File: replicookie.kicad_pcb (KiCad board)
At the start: 2 copper layers, 152.4 x 101.6 mm, 8 parts, among them P2 TFM-115-01-F-D-A, P3 TFM-120-01-F-D-A

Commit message: Annotate schematic
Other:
- net class Default removed

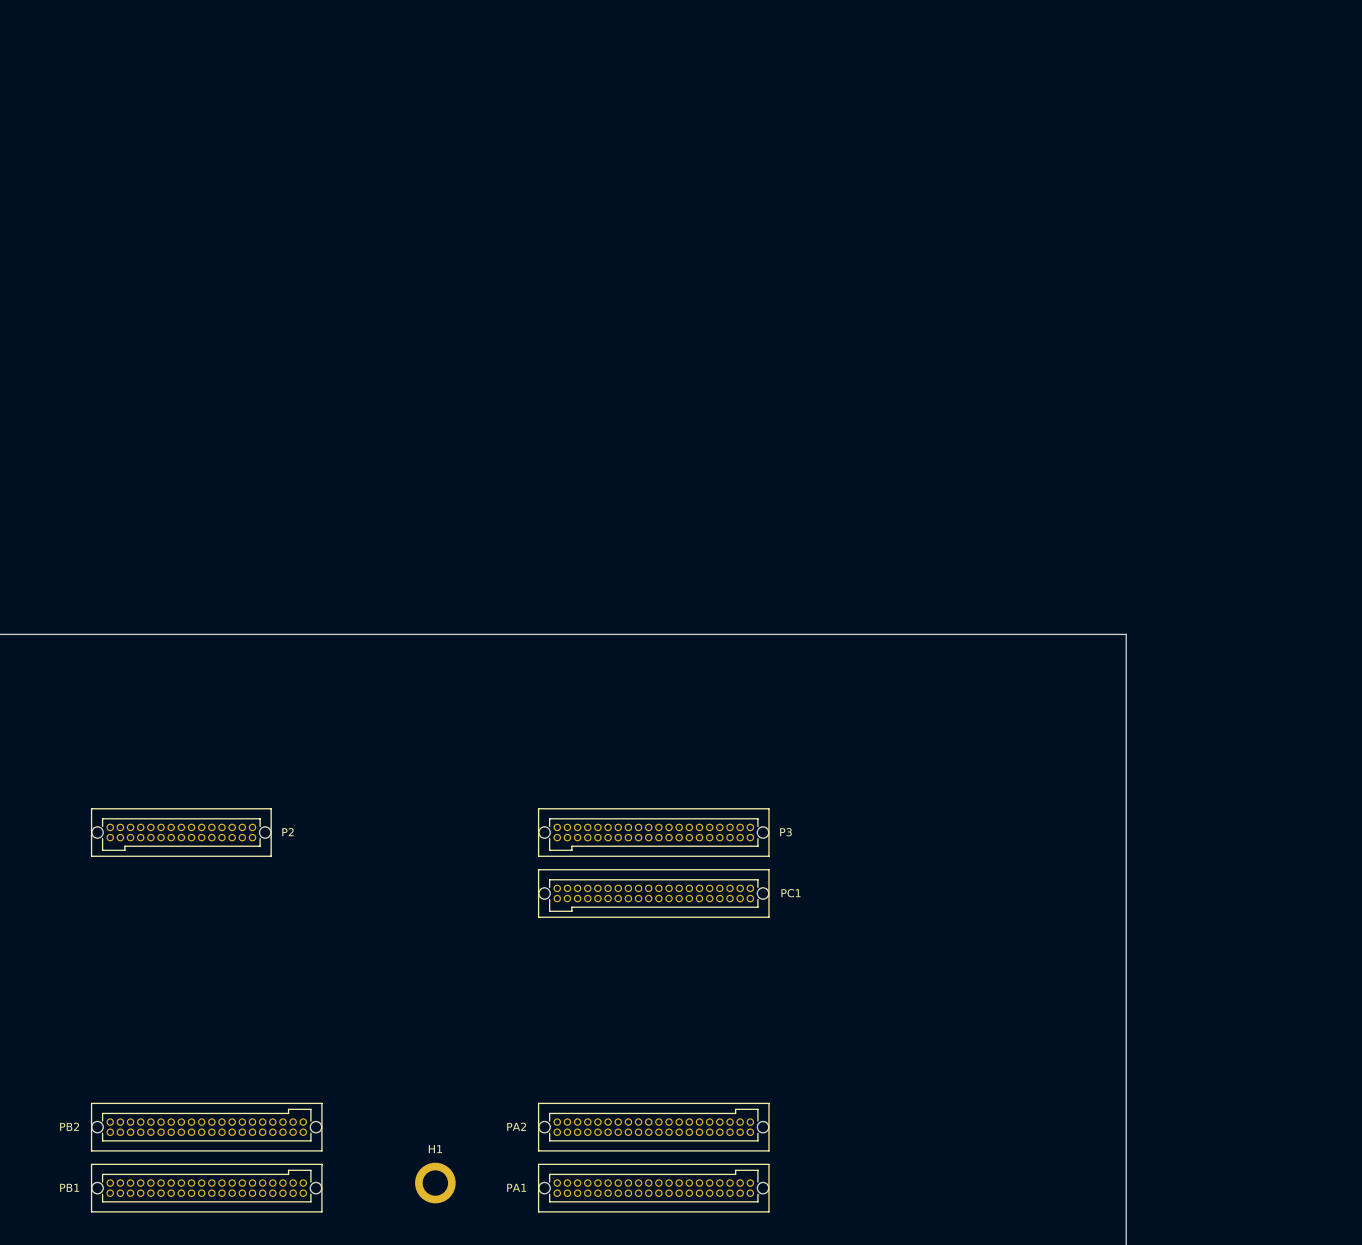
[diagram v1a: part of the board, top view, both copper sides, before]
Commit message: Fix footprint associations, use 74LVC2G07 instead of MOSFETs
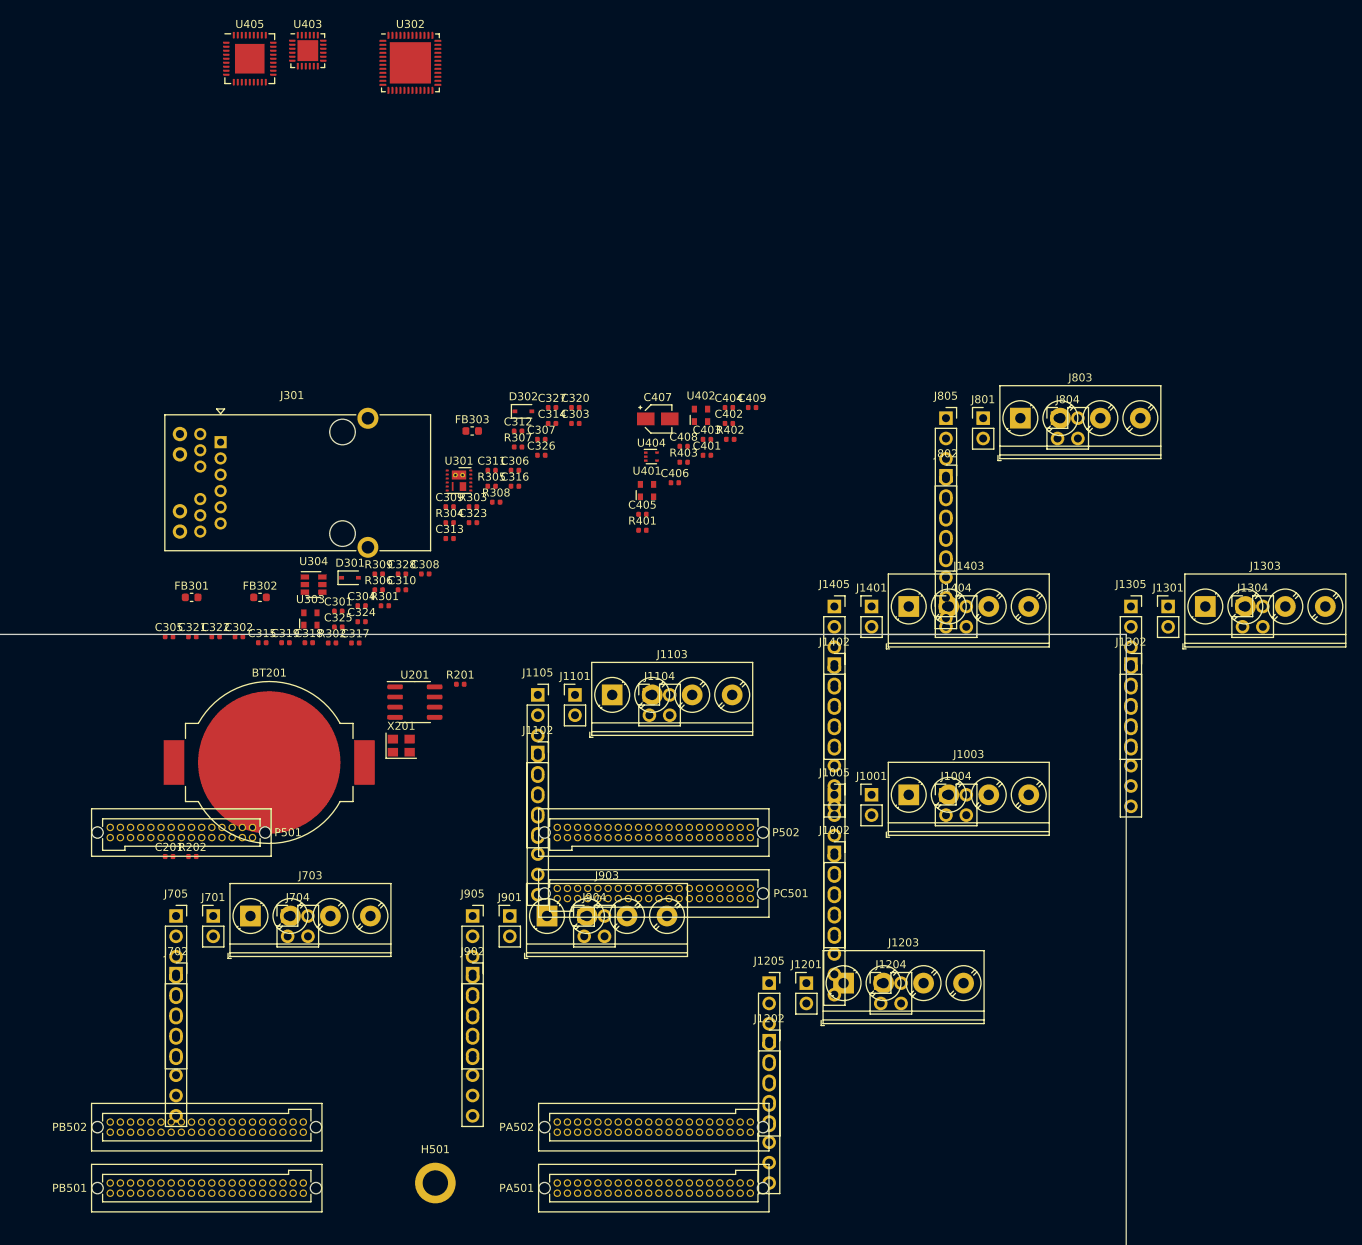
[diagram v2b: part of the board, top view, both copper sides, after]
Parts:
- added BT201: Battery_Cell, Battery:BatteryHolder_MPD_BC2003_1x2032, F.Cu at (83.4, 54.1)
- added C201: 0.01u, Capacitor_SMD:C_0402_1005Metric, F.Cu at (70.9, 65.9)
- added C301: 4.7u, Capacitor_SMD:C_0402_1005Metric, F.Cu at (92.0, 35.2)
- added C302: 560p, Capacitor_SMD:C_0402_1005Metric, F.Cu at (79.6, 38.4)
- added C303: 10u, Capacitor_SMD:C_0402_1005Metric, F.Cu at (121.6, 11.7)
- added C304: 10u, Capacitor_SMD:C_0402_1005Metric, F.Cu at (94.9, 34.5)
- added C305: 10u, Capacitor_SMD:C_0402_1005Metric, F.Cu at (70.9, 38.4)
- added C306: 0.1U, Capacitor_SMD:C_0402_1005Metric, F.Cu at (114.1, 17.6)
- added C307: 10u, Capacitor_SMD:C_0402_1005Metric, F.Cu at (117.4, 13.7)
- added C308: 10u, Capacitor_SMD:C_0402_1005Metric, F.Cu at (102.9, 30.5)
- added C309: 0.1U, Capacitor_SMD:C_0402_1005Metric, F.Cu at (105.9, 22.1)
- added C310: 0.1U, Capacitor_SMD:C_0402_1005Metric, F.Cu at (100.0, 32.5)
- added C311: 0.1U, Capacitor_SMD:C_0402_1005Metric, F.Cu at (111.2, 17.6)
- added C312: 0.1U, Capacitor_SMD:C_0402_1005Metric, F.Cu at (114.5, 12.7)
- added C313: 0.1U, Capacitor_SMD:C_0402_1005Metric, F.Cu at (105.9, 26.1)
- added C314: 0.1U, Capacitor_SMD:C_0402_1005Metric, F.Cu at (118.7, 11.7)
- added C315: 0.1U, Capacitor_SMD:C_0402_1005Metric, F.Cu at (82.5, 39.1)
- added C316: 0.1U, Capacitor_SMD:C_0402_1005Metric, F.Cu at (114.1, 19.6)
- added C317: 0.1U, Capacitor_SMD:C_0402_1005Metric, F.Cu at (94.1, 39.2)
- added C318: 0.1U, Capacitor_SMD:C_0402_1005Metric, F.Cu at (88.3, 39.1)
- added C319: 0.1U, Capacitor_SMD:C_0402_1005Metric, F.Cu at (85.4, 39.1)
- added C320: 0.01u, Capacitor_SMD:C_0402_1005Metric, F.Cu at (121.6, 9.74)
- added C321: 0.1U, Capacitor_SMD:C_0402_1005Metric, F.Cu at (73.8, 38.4)
- added C322: 10u, Capacitor_SMD:C_0402_1005Metric, F.Cu at (76.7, 38.4)
- added C323: 0.1u, Capacitor_SMD:C_0402_1005Metric, F.Cu at (108.8, 24.1)
- added C324: 0.1u, Capacitor_SMD:C_0402_1005Metric, F.Cu at (94.9, 36.5)
- added C325: 10u, Capacitor_SMD:C_0402_1005Metric, F.Cu at (92.0, 37.2)
- added C326: 0.1u, Capacitor_SMD:C_0402_1005Metric, F.Cu at (117.4, 15.7)
- added C327: 0.1U, Capacitor_SMD:C_0402_1005Metric, F.Cu at (118.7, 9.74)
- added C328: 0.1u, Capacitor_SMD:C_0402_1005Metric, F.Cu at (100.0, 30.5)
- added C401: 0.01u, Capacitor_SMD:C_0402_1005Metric, F.Cu at (138.1, 15.7)
- added C402: 0.01u, Capacitor_SMD:C_0402_1005Metric, F.Cu at (140.8, 11.7)
- added C403: 1u, Capacitor_SMD:C_0402_1005Metric, F.Cu at (138.1, 13.7)
- added C404: 0.1u, Capacitor_SMD:C_0402_1005Metric, F.Cu at (140.8, 9.74)
- added C405: 0.1u, Capacitor_SMD:C_0402_1005Metric, F.Cu at (130.0, 23.1)
- added C406: 1u, Capacitor_SMD:C_0402_1005Metric, F.Cu at (134.1, 19.1)
- added C407: 150u, Capacitor_SMD:CP_Elec_3x5.3, F.Cu at (131.9, 11.2)
- added C408: 0.1u, Capacitor_SMD:C_0402_1005Metric, F.Cu at (135.2, 14.6)
- added C409: 0.1u, Capacitor_SMD:C_0402_1005Metric, F.Cu at (143.7, 9.74)
- added D301: 1N4148WS, Diode_SMD:D_SOD-323, F.Cu at (93.5, 31.0)
- added D302: 1N4148WS, Diode_SMD:D_SOD-323, F.Cu at (115.1, 10.2)
- added FB301: 100 ohms, Inductor_SMD:L_0603_1608Metric, F.Cu at (73.7, 33.5)
- added FB302: 100 ohms, Inductor_SMD:L_0603_1608Metric, F.Cu at (82.2, 33.5)
- added FB303: 100 ohms, Inductor_SMD:L_0603_1608Metric, F.Cu at (108.7, 12.7)
- added J1001: Conn_01x02_Male, Connector_PinHeader_2.54mm:PinHeader_1x02_P2.54mm_Vertical, F.Cu at (158.7, 58.2)
- added J1002: Conn_01x08_Female, Connector_PinSocket_2.54mm:PinSocket_1x08_P2.54mm_Vertical, F.Cu at (154.0, 65.4)
- added J1003: Screw_Terminal_01x04, TerminalBlock_Phoenix:TerminalBlock_Phoenix_PT-1,5-4-5.0-H_1x04_P5.00mm_Horizontal, F.Cu at (163.3, 58.2)
- added J1004: Conn_02x02_Odd_Even, Connector_PinHeader_2.54mm:PinHeader_2x02_P2.54mm_Vertical, F.Cu at (168.0, 58.2)
- added J1005: Conn_01x08_Female, Connector_PinSocket_2.54mm:PinSocket_1x08_P2.54mm_Vertical, F.Cu at (154.0, 58.2)
- added J1101: Conn_01x02_Male, Connector_PinHeader_2.54mm:PinHeader_1x02_P2.54mm_Vertical, F.Cu at (121.6, 45.7)
- added J1102: Conn_01x08_Female, Connector_PinSocket_2.54mm:PinSocket_1x08_P2.54mm_Vertical, F.Cu at (116.9, 52.9)
- added J1103: Screw_Terminal_01x04, TerminalBlock_Phoenix:TerminalBlock_Phoenix_PT-1,5-4-5.0-H_1x04_P5.00mm_Horizontal, F.Cu at (126.2, 45.7)
- added J1104: Conn_02x02_Odd_Even, Connector_PinHeader_2.54mm:PinHeader_2x02_P2.54mm_Vertical, F.Cu at (130.9, 45.7)
- added J1105: Conn_01x08_Female, Connector_PinSocket_2.54mm:PinSocket_1x08_P2.54mm_Vertical, F.Cu at (116.9, 45.7)
- added J1201: Conn_01x02_Male, Connector_PinHeader_2.54mm:PinHeader_1x02_P2.54mm_Vertical, F.Cu at (150.5, 81.7)
- added J1202: Conn_01x08_Female, Connector_PinSocket_2.54mm:PinSocket_1x08_P2.54mm_Vertical, F.Cu at (145.9, 88.9)
- added J1203: Screw_Terminal_01x04, TerminalBlock_Phoenix:TerminalBlock_Phoenix_PT-1,5-4-5.0-H_1x04_P5.00mm_Horizontal, F.Cu at (155.2, 81.7)
- added J1204: Conn_02x02_Odd_Even, Connector_PinHeader_2.54mm:PinHeader_2x02_P2.54mm_Vertical, F.Cu at (159.8, 81.7)
- added J1205: Conn_01x08_Female, Connector_PinSocket_2.54mm:PinSocket_1x08_P2.54mm_Vertical, F.Cu at (145.9, 81.7)
- added J1301: Conn_01x02_Male, Connector_PinHeader_2.54mm:PinHeader_1x02_P2.54mm_Vertical, F.Cu at (195.7, 34.6)
- added J1302: Conn_01x08_Female, Connector_PinSocket_2.54mm:PinSocket_1x08_P2.54mm_Vertical, F.Cu at (191.1, 41.8)
- added J1303: Screw_Terminal_01x04, TerminalBlock_Phoenix:TerminalBlock_Phoenix_PT-1,5-4-5.0-H_1x04_P5.00mm_Horizontal, F.Cu at (200.4, 34.6)
- added J1304: Conn_02x02_Odd_Even, Connector_PinHeader_2.54mm:PinHeader_2x02_P2.54mm_Vertical, F.Cu at (205.0, 34.6)
- added J1305: Conn_01x08_Female, Connector_PinSocket_2.54mm:PinSocket_1x08_P2.54mm_Vertical, F.Cu at (191.1, 34.6)
- added J1401: Conn_01x02_Male, Connector_PinHeader_2.54mm:PinHeader_1x02_P2.54mm_Vertical, F.Cu at (158.7, 34.6)
- added J1402: Conn_01x08_Female, Connector_PinSocket_2.54mm:PinSocket_1x08_P2.54mm_Vertical, F.Cu at (154.0, 41.8)
- added J1403: Screw_Terminal_01x04, TerminalBlock_Phoenix:TerminalBlock_Phoenix_PT-1,5-4-5.0-H_1x04_P5.00mm_Horizontal, F.Cu at (163.3, 34.6)
- added J1404: Conn_02x02_Odd_Even, Connector_PinHeader_2.54mm:PinHeader_2x02_P2.54mm_Vertical, F.Cu at (168.0, 34.6)
- added J1405: Conn_01x08_Female, Connector_PinSocket_2.54mm:PinSocket_1x08_P2.54mm_Vertical, F.Cu at (154.0, 34.6)
- added J301: JK0654219, Connector_RJ:RJ45_Pulse_JK0654219NL_Horizontal, F.Cu at (77.3, 14.1)
- added J701: Conn_01x02_Male, Connector_PinHeader_2.54mm:PinHeader_1x02_P2.54mm_Vertical, F.Cu at (76.4, 73.3)
- added J702: Conn_01x08_Female, Connector_PinSocket_2.54mm:PinSocket_1x08_P2.54mm_Vertical, F.Cu at (71.7, 80.5)
- added J703: Screw_Terminal_01x04, TerminalBlock_Phoenix:TerminalBlock_Phoenix_PT-1,5-4-5.0-H_1x04_P5.00mm_Horizontal, F.Cu at (81.0, 73.3)
- added J704: Conn_02x02_Odd_Even, Connector_PinHeader_2.54mm:PinHeader_2x02_P2.54mm_Vertical, F.Cu at (85.7, 73.3)
- added J705: Conn_01x08_Female, Connector_PinSocket_2.54mm:PinSocket_1x08_P2.54mm_Vertical, F.Cu at (71.7, 73.3)
- added J801: Conn_01x02_Male, Connector_PinHeader_2.54mm:PinHeader_1x02_P2.54mm_Vertical, F.Cu at (172.6, 11.1)
- added J802: Conn_01x08_Female, Connector_PinSocket_2.54mm:PinSocket_1x08_P2.54mm_Vertical, F.Cu at (168.0, 18.3)
- added J803: Screw_Terminal_01x04, TerminalBlock_Phoenix:TerminalBlock_Phoenix_PT-1,5-4-5.0-H_1x04_P5.00mm_Horizontal, F.Cu at (177.3, 11.1)
- added J804: Conn_02x02_Odd_Even, Connector_PinHeader_2.54mm:PinHeader_2x02_P2.54mm_Vertical, F.Cu at (181.9, 11.1)
- added J805: Conn_01x08_Female, Connector_PinSocket_2.54mm:PinSocket_1x08_P2.54mm_Vertical, F.Cu at (168.0, 11.1)
- added J901: Conn_01x02_Male, Connector_PinHeader_2.54mm:PinHeader_1x02_P2.54mm_Vertical, F.Cu at (113.4, 73.3)
- added J902: Conn_01x08_Female, Connector_PinSocket_2.54mm:PinSocket_1x08_P2.54mm_Vertical, F.Cu at (108.8, 80.5)
- added J903: Screw_Terminal_01x04, TerminalBlock_Phoenix:TerminalBlock_Phoenix_PT-1,5-4-5.0-H_1x04_P5.00mm_Horizontal, F.Cu at (118.1, 73.3)
- added J904: Conn_02x02_Odd_Even, Connector_PinHeader_2.54mm:PinHeader_2x02_P2.54mm_Vertical, F.Cu at (122.7, 73.3)
- added J905: Conn_01x08_Female, Connector_PinSocket_2.54mm:PinSocket_1x08_P2.54mm_Vertical, F.Cu at (108.8, 73.3)
- added R201: 2k, Resistor_SMD:R_0402_1005Metric, F.Cu at (107.3, 44.3)
- added R202: 2k, Resistor_SMD:R_0402_1005Metric, F.Cu at (73.8, 65.9)
- added R301: 10k, Resistor_SMD:R_0402_1005Metric, F.Cu at (97.8, 34.5)
- added R302: 4.7k, Resistor_SMD:R_0402_1005Metric, F.Cu at (91.2, 39.2)
- added R303: 1k, Resistor_SMD:R_0402_1005Metric, F.Cu at (108.8, 22.1)
- added R304: 1.5k, Resistor_SMD:R_0402_1005Metric, F.Cu at (105.9, 24.1)
- added R305: 1k, Resistor_SMD:R_0402_1005Metric, F.Cu at (111.2, 19.6)
- added R306: 12.1k, Resistor_SMD:R_0402_1005Metric, F.Cu at (97.1, 32.5)
- added R307: 10k, Resistor_SMD:R_0402_1005Metric, F.Cu at (114.5, 14.7)
- added R308: 75, Resistor_SMD:R_0402_1005Metric, F.Cu at (111.7, 21.6)
- added R309: 75, Resistor_SMD:R_0402_1005Metric, F.Cu at (97.1, 30.5)
- added R401: 8.06k 1%, Resistor_SMD:R_0402_1005Metric, F.Cu at (130.0, 25.1)
- added R402: 10k 1/16W, Resistor_SMD:R_0402_1005Metric, F.Cu at (141.0, 13.7)
- added R403: 12k, Resistor_SMD:R_0402_1005Metric, F.Cu at (135.2, 16.6)
- added U201: DS1307ZN+, Package_SO:SOIC-8_3.9x4.9mm_P1.27mm, F.Cu at (101.6, 46.6)
- added U301: MIC33050-4YHL, Package_DFN_QFN:HDFN-12-1EP_3x3mm_P0.5mm_EP1.8x1.125mm, F.Cu at (107.1, 18.9)
- added U302: KSZ9031RNXCA, Package_DFN_QFN:QFN-48-1EP_7x7mm_P0.5mm_EP5.15x5.15mm, F.Cu at (101.0, -33.3)
- added U303: ASDMB-25.000MHz, Oscillator:Oscillator_SMD_Abracon_ASDMB-4Pin_2.5x2.0mm, F.Cu at (88.5, 36.2)
- added U304: 74LVC2G07, Package_TO_SOT_SMD:SOT-23-6, F.Cu at (88.9, 31.9)
- added U401: ASDMB-24.000MHz-C, Oscillator:Oscillator_SMD_Abracon_ASDMB-4Pin_2.5x2.0mm, F.Cu at (130.6, 20.1)
- added U402: ASDMB-26.000MHz-C, Oscillator:Oscillator_SMD_Abracon_ASDMB-4Pin_2.5x2.0mm, F.Cu at (137.3, 10.7)
- added U403: USB3343, Package_DFN_QFN:QFN-24-1EP_4x4mm_P0.5mm_EP2.6x2.6mm, F.Cu at (88.2, -34.9)
- added U404: 74LVC1G07, Package_TO_SOT_SMD:SOT-553, F.Cu at (131.1, 15.9)
- added U405: USB2514B_Bi, Package_DFN_QFN:QFN-36-1EP_6x6mm_P0.5mm_EP3.7x3.7mm, F.Cu at (80.9, -33.9)
- added X201: ASE-xxxMHz, Oscillator:Oscillator_SMD_Abracon_ASE-4Pin_3.2x2.5mm, F.Cu at (99.9, 52.0)
- renumbered H1 to H501, P2 to P501, P3 to P502, PA1 to PA501, PA2 to PA502, PB1 to PB501, PB2 to PB502, PC1 to PC501

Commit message: Connect Ethernet and USB to MIO, start layout
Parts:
- removed BT201: Battery_Cell, Battery:BatteryHolder_MPD_BC2003_1x2032
- removed J1004, J1104, J1204, J1304, J1404, J704, J804, J904: Conn_02x02_Odd_Even, Connector_PinHeader_2.54mm:PinHeader_2x02_P2.54mm_Vertical
- added C1001: 100u 35V, Capacitor_SMD:CP_Elec_5x3, F.Cu at (101.0, -107.3)
- added C1101: 100u 35V, Capacitor_SMD:CP_Elec_5x3, F.Cu at (58.9, -93.7)
- added C1201: 100u 35V, Capacitor_SMD:CP_Elec_5x3, F.Cu at (101.0, -93.7)
- added C1301: 100u 35V, Capacitor_SMD:CP_Elec_5x3, F.Cu at (79.9, -80.1)
- added C1401: 100u 35V, Capacitor_SMD:CP_Elec_5x3, F.Cu at (79.9, -93.7)
- added C329: 0.1u, Capacitor_SMD:C_0603_1608Metric, F.Cu at (181.8, -98.1)
- added C330: 0.1u, Capacitor_SMD:C_0603_1608Metric, F.Cu at (181.8, -96.1)
- added C701: 100u 35V, Capacitor_SMD:CP_Elec_5x3, F.Cu at (48.3, 133.3)
- added C801: 100u 35V, Capacitor_SMD:CP_Elec_5x3, F.Cu at (79.9, -107.3)
- added C901: 100u 35V, Capacitor_SMD:CP_Elec_5x3, F.Cu at (58.9, -80.1)
- added J401: USB_A, Connector_USB:USB_A_Molex_67643_Horizontal, F.Cu at (137.3, -95.8)
- added J402: USB_A, Connector_USB:USB_A_Molex_67643_Horizontal, F.Cu at (155.5, -95.8)
- added R1001: 10k, Resistor_SMD:R_0603_1608Metric, F.Cu at (108.8, -111.0)
- added R1101: 10k, Resistor_SMD:R_0603_1608Metric, F.Cu at (66.7, -97.4)
- added R1201: 10k, Resistor_SMD:R_0603_1608Metric, F.Cu at (108.8, -97.4)
- added R1301: 10k, Resistor_SMD:R_0603_1608Metric, F.Cu at (87.8, -83.8)
- added R1401: 10k, Resistor_SMD:R_0603_1608Metric, F.Cu at (87.8, -97.4)
- added R701: 10k, Resistor_SMD:R_0603_1608Metric, F.Cu at (66.7, -111.0)
- added R801: 10k, Resistor_SMD:R_0603_1608Metric, F.Cu at (87.8, -111.0)
- added R901: 10k, Resistor_SMD:R_0603_1608Metric, F.Cu at (66.7, -83.8)
- added U305: TXS0102DCU, Package_SO:VSSOP-8_2.3x2mm_P0.5mm, F.Cu at (177.6, -97.3)
- C201, C301, C302, C303, C304, C305, C306, C307, C308, C309, C310, C311, C312, C313, C314, C315, C316, C317, C318, C319, C320, C321, C322, C323, C324, C325, C326, C327, C328, C401, C402, C403, C404, C405, C406, C408, C409: footprint Capacitor_SMD:C_0402_1005Metric -> Capacitor_SMD:C_0603_1608Metric
- J1001, J1101, J1201, J1301, J1401, J701, J801, J901: value Conn_01x02_Male -> Conn_02x03_Odd_Even; footprint Connector_PinHeader_2.54mm:PinHeader_1x02_P2.54mm_Vertical -> Connector_PinHeader_2.54mm:PinHeader_2x03_P2.54mm_Vertical
- R201, R202, R301, R302, R303, R304, R305, R306, R307, R308, R309, R401, R402, R403: footprint Resistor_SMD:R_0402_1005Metric -> Resistor_SMD:R_0603_1608Metric
- moved J802 145.5 mm to (61.0, 116.8)
- moved J801 114.1 mm to (70.3, 61.5)
- moved J1301 96.6 mm to (103.0, 61.5)
- moved J1302 82.7 mm to (156.2, 116.8)
- moved J703 82.6 mm to (41.9, 146.1)
- moved J1402 78.0 mm to (175.3, 116.8)
- moved J1401 76.9 mm to (86.6, 61.5)
- moved J1002 75.3 mm to (99.1, 116.8)
- moved J1001 74.0 mm to (86.6, 75.0)
- moved J1101 73.8 mm to (53.9, 75.0)
- moved J1102 64.0 mm to (118.1, 116.8)
- moved J301 59.3 mm to (44.5, 63.5), turned to 90 degrees
- moved J701 49.9 mm to (52.1, 116.8), turned to -90 degrees
- moved J1201 48.0 mm to (103.0, 75.0)
- moved J702 47.0 mm to (41.9, 116.8)
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- renumbered P501 to P2, P502 to P3, PA501 to PA1, PA502 to PA2, PB501 to PB1, PB502 to PB2, PC501 to PC1
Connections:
- net /USB/~RESET renamed /~RESET_1
- net Net-(P502-Pad2) renamed /Snickerdoodle/~ETHERNET_RST
- net Net-(P502-Pad4) renamed /Snickerdoodle/~USB_RST
- J1001 pad 1: GNDD -> +3V3
- J1001 pad 2: GNDD -> +3V3
- J1101 pad 1: GNDD -> +3V3
- J1101 pad 2: GNDD -> +3V3
- J1201 pad 1: GNDD -> +3V3
- J1201 pad 2: GNDD -> +3V3
- J1301 pad 1: GNDD -> +3V3
- J1301 pad 2: GNDD -> +3V3
- J1401 pad 1: GNDD -> +3V3
- J1401 pad 2: GNDD -> +3V3
- J701 pad 1: GNDD -> +3V3
- J701 pad 2: GNDD -> +3V3
- J801 pad 1: GNDD -> +3V3
- J801 pad 2: GNDD -> +3V3
- J901 pad 1: GNDD -> +3V3
- J901 pad 2: GNDD -> +3V3
- P3 pad 11: Net-(P502-Pad11) -> /ETHERNET.TXD3
- P3 pad 12: Net-(P502-Pad12) -> /ETHERNET.RXD0
- P3 pad 13: Net-(P502-Pad13) -> /ETHERNET.TX_CTL
- P3 pad 14: Net-(P502-Pad14) -> /ETHERNET.RX_CLK
- P3 pad 17: Net-(P502-Pad17) -> /ETHERNET.RXD1
- P3 pad 18: Net-(P502-Pad18) -> /ETHERNET.RX_CTL
- P3 pad 19: Net-(P502-Pad19) -> /ETHERNET.RXD2
- P3 pad 20: Net-(P502-Pad20) -> /ETHERNET.RXD3
- P3 pad 23: Net-(P502-Pad23) -> /USB.DATA4
- P3 pad 24: Net-(P502-Pad24) -> /USB.NXT
- P3 pad 25: Net-(P502-Pad25) -> /USB.DIR
- P3 pad 26: Net-(P502-Pad26) -> /USB.STP
- P3 pad 29: Net-(P502-Pad29) -> /USB.DATA0
- P3 pad 30: Net-(P502-Pad30) -> /USB.DATA3
- P3 pad 31: Net-(P502-Pad31) -> /USB.DATA1
- P3 pad 32: Net-(P502-Pad32) -> /USB.DATA2
- P3 pad 35: Net-(P502-Pad35) -> /USB.CLK
- P3 pad 36: Net-(P502-Pad36) -> /USB.DATA7
- P3 pad 37: Net-(P502-Pad37) -> /USB.DATA5
- P3 pad 38: Net-(P502-Pad38) -> /USB.DATA6
- P3 pad 5: Net-(P502-Pad5) -> /ETHERNET.TX_CLK
- P3 pad 6: Net-(P502-Pad6) -> /ETHERNET.TXD2
- P3 pad 7: Net-(P502-Pad7) -> /ETHERNET.TXD0
- P3 pad 8: Net-(P502-Pad8) -> /ETHERNET.TXD1
- PA2 pad 36: Net-(PA502-Pad36) -> /ETHERNET.MDC
- PA2 pad 38: Net-(PA502-Pad38) -> /ETHERNET.MDIO
- U302 pad 19: /Ethernet/TXD0 -> /ETHERNET.TXD0
- U302 pad 20: /Ethernet/TXD1 -> /ETHERNET.TXD1
- U302 pad 21: /Ethernet/TXD2 -> /ETHERNET.TXD2
- U302 pad 22: /Ethernet/TXD3 -> /ETHERNET.TXD3
- U302 pad 24: /Ethernet/TX_CLK -> /ETHERNET.TX_CLK
- U302 pad 25: /Ethernet/TX_CTL -> /ETHERNET.TX_CTL
- U302 pad 27: /Ethernet/RXD3 -> /ETHERNET.RXD3
- U302 pad 28: /Ethernet/RXD2 -> /ETHERNET.RXD2
- U302 pad 31: /Ethernet/RXD1 -> /ETHERNET.RXD1
- U302 pad 32: /Ethernet/RXD0 -> /ETHERNET.RXD0
- U302 pad 33: /Ethernet/RX_CTL -> /ETHERNET.RX_CTL
- U302 pad 35: /Ethernet/RX_CLK -> /ETHERNET.RX_CLK
- U405 pad 1: Net-(U405-Pad1) -> /USB/D1P
- U405 pad 2: Net-(U405-Pad2) -> /USB/D1N
- U405 pad 3: Net-(U405-Pad3) -> /USB/D2P
- U405 pad 4: Net-(U405-Pad4) -> /USB/D2N
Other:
- board size 152.4 x 101.6 mm -> 152.4 x 114.3 mm
